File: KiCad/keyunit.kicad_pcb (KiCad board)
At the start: 2 copper layers, 79.1 x 18 mm, 29 parts, among them J1 Conn_01x03_Male, J3 Conn_01x05_Male, J5 Conn_01x05_Male, SW0 SW_Push

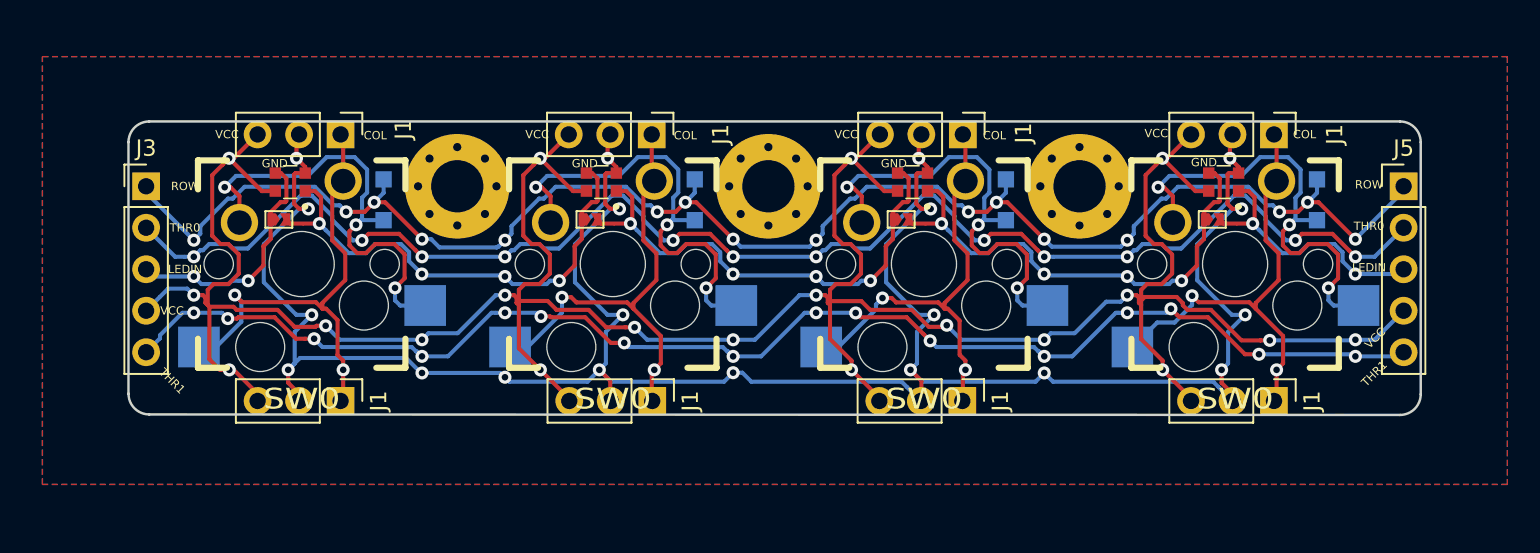
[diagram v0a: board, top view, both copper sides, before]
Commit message: Add keyunit foot print and keyunit2 board
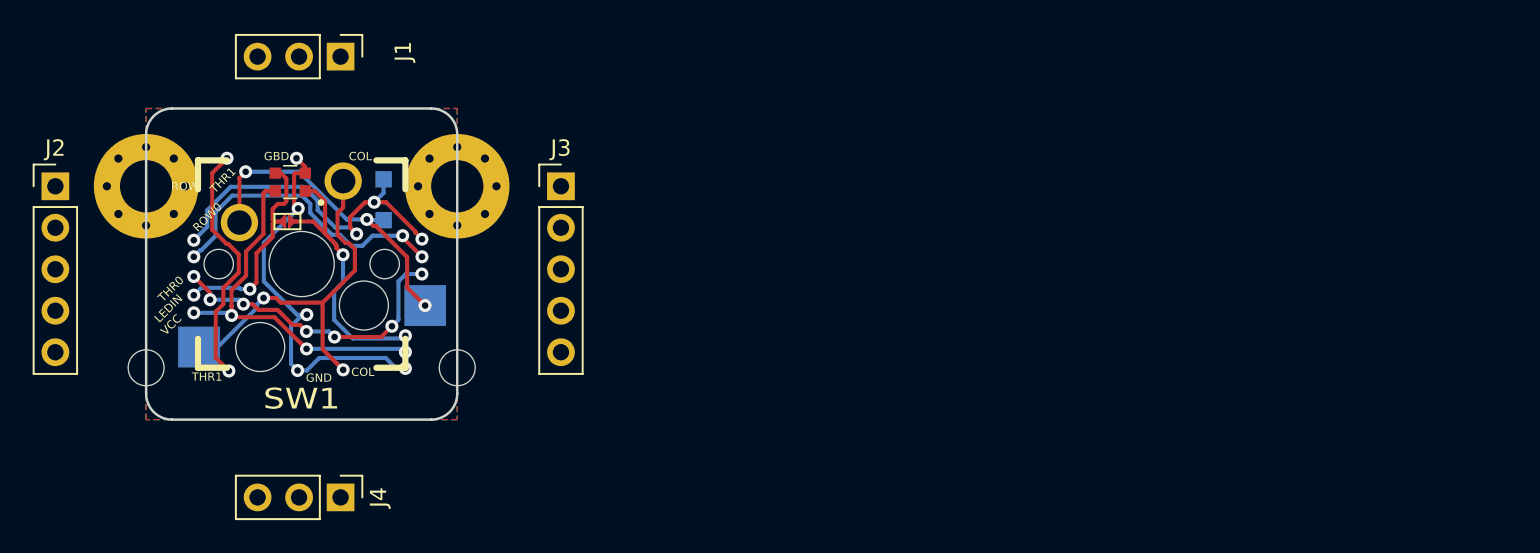
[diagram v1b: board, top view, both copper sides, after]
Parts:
- removed the D1 at (86.7, 66.5)
- removed the D1 at (67.6, 66.5)
- removed the D1 at (48.6, 66.5)
- removed the J1 at (46.0, 78.9)
- removed the J1 at (65.0, 78.9)
- removed the J1 at (84.0, 78.9)
- removed the J1 at (26.9, 78.9)
- removed the J1 at (84.0, 62.5)
- removed the J1 at (65.0, 62.5)
- removed the J1 at (45.9, 62.5)
- removed J5: Conn_01x05_Male, Connector_PinHeader_2.54mm:PinHeader_1x05_P2.54mm_Vertical
- removed the LED1 at (81.0, 65.5)
- removed the LED1 at (61.9, 65.5)
- removed the LED1 at (42.9, 65.5)
- removed the REF** at (80.1, 67.8)
- removed the REF** at (72.1, 65.7)
- removed the REF** at (61.0, 67.8)
- removed the REF** at (53.1, 65.7)
- removed the REF** at (42.0, 67.8)
- removed the REF** at (22.9, 67.8)
- removed SW0 (x3): SW_Push, HKB44:MX_PCB_100H_socket
- added J3: Conn_01x05_Male, Connector_PinHeader_2.54mm:PinHeader_1x05_P2.54mm_Vertical, F.Cu at (40.4, 65.7)
- added J4: Conn_01x03_Male, Connector_PinHeader_2.54mm:PinHeader_1x03_P2.54mm_Vertical, F.Cu at (26.9, 84.8)
- added JP1: Jumper_NO_Small, library:SolderJumper-2_small, F.Cu at (23.6, 67.9)
- added REF**: MountingHole_2.2mm_M2_DIN965, MountingHole:MountingHole_2.2mm_M2_DIN965, F.Cu at (15.0, 76.8)
- added REF**: MountingHole_2.2mm_M2_DIN965, MountingHole:MountingHole_2.2mm_M2_DIN965, F.Cu at (34.0, 76.8)
- added REF**: MountingHole_3.2mm_M3_Pad_Via, MountingHole:MountingHole_3.2mm_M3_Pad_Via, F.Cu at (15.0, 65.7)
- moved J2 5.56 mm to (9.43, 65.7)
- moved J1 4.76 mm to (26.9, 57.8)
- renumbered J3 to J2, SW0 to SW1
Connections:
- J1 pad 3: VCC -> through2
- J2 pad 3: LEDIN -> through
- J2 pad 4: VCC -> LEDIN
- J2 pad 5: through -> VCC
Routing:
- net VCC: track 187.0 -> 23.0 mm, vias 20 -> 4
- net GND: track 148.4 -> 23.9 mm, vias 20 -> 5
- net Net-(D1-Pad2): track 114.3 -> 19.8 mm, vias 12 -> 3
- net COL0: track 111.0 -> 23.8 mm, vias 8 -> 2
- net ROW0: track 103.0 -> 22.4 mm, vias 16 -> 4
- net ROW1: track 93.6 -> 18.7 mm, vias 12 -> 3
- net through: track 86.2 -> 18.7 mm, vias 16 -> 7
- net LEDIN: track 50.4 -> 12.7 mm, vias 8 -> 2
- net LEDOUT: track 47.6 -> 17.4 mm, vias 8 -> 2
- net (no net): track 23.2 -> 0.00 mm
- net through2: track 0.00 -> 15.0 mm, vias 0 -> 2
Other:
- board size 79.1 x 18 mm -> 19.1 x 19.1 mm
- board text added: "GBD"
- board text added: "ROW0"
